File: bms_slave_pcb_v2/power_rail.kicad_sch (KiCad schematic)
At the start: 19 parts, among them Q13 2N7002, U5 LT3990HMSEI-5I-PBF

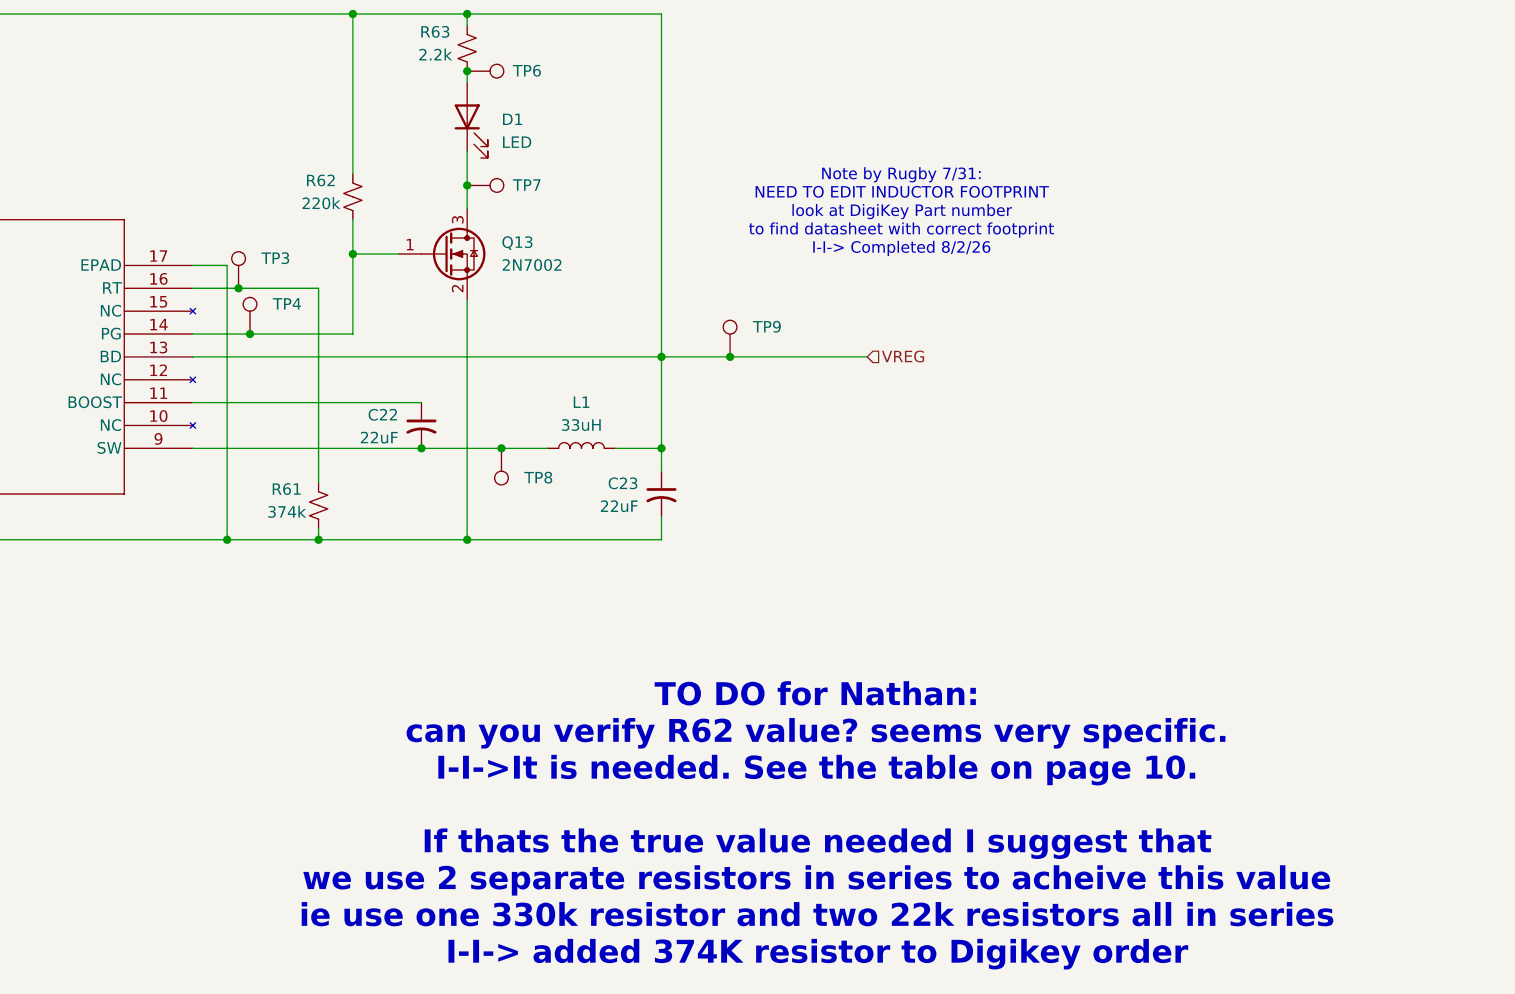
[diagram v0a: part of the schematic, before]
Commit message: Fixed filenames in BMS Slave PCB V2.01, added equipment wishlist
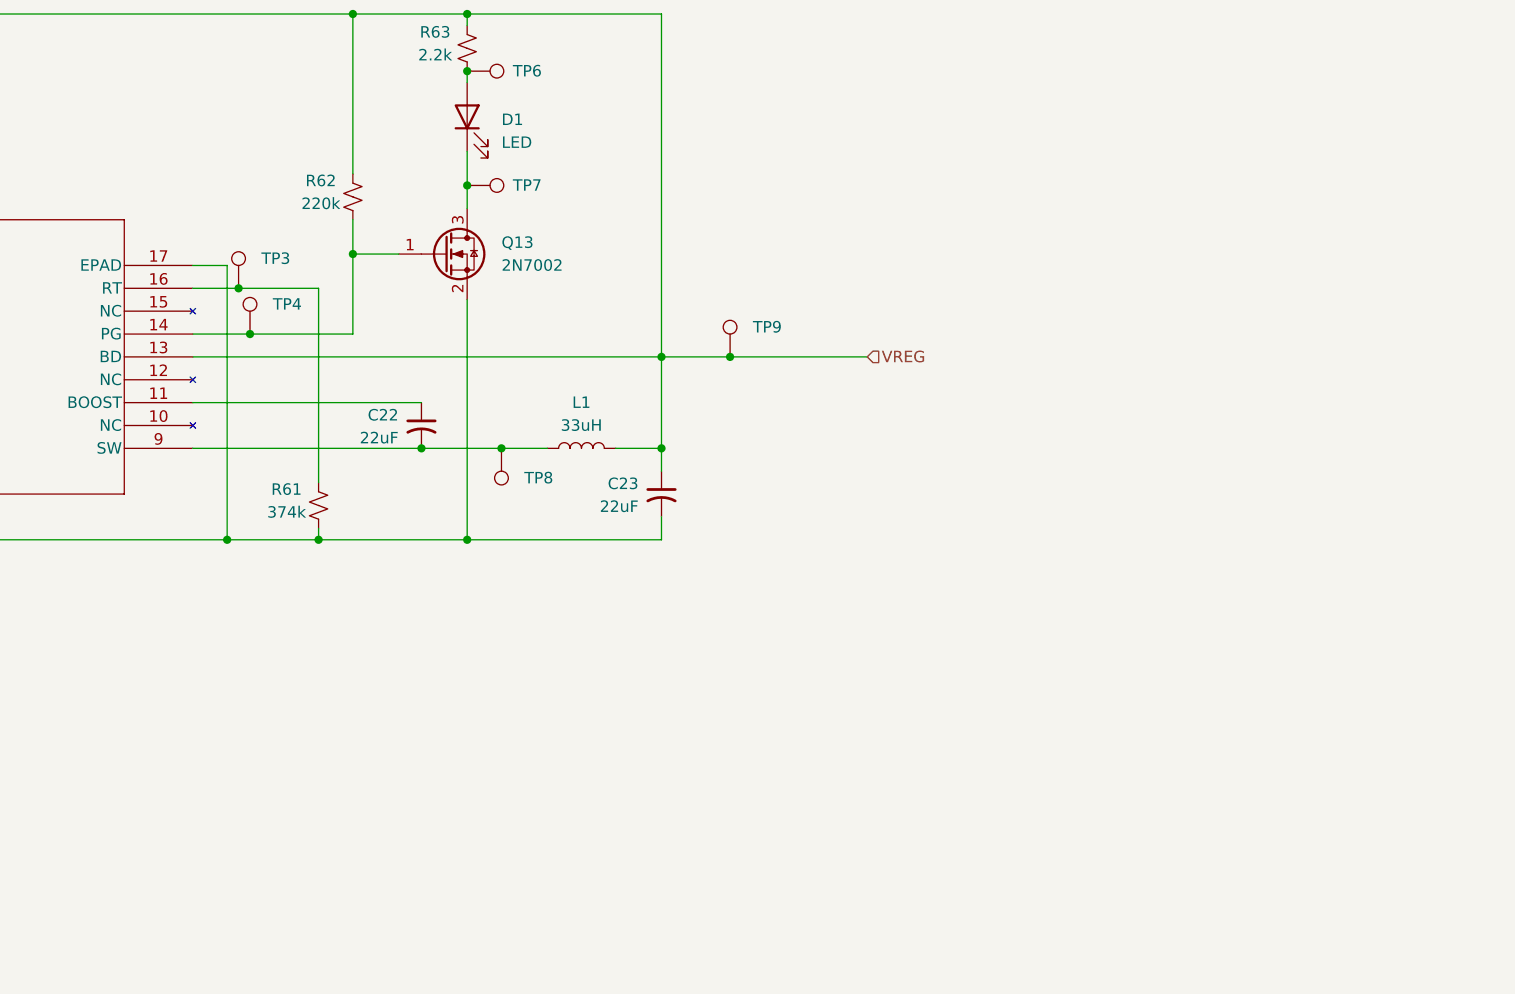
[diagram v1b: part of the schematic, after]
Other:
- note removed: "Note by Rugby 7/31: NEED TO EDIT INDUCTOR FOOTPRINT look at DigiKey Part number to find datasheet with correct footprint I-I-> Completed 8/2/26"
- note removed: "TO DO for Nathan: can you verify R62 value? seems very specific. I-I->It is needed. See the table on page 10. If thats the true value needed I suggest that we use 2 separate resistors in series to acheive this value ie use one 330k resistor and two 22k resistors all in series I-I-> added 374K resistor to Digikey order"
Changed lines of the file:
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@@
-		)
-	)
-	(text "Note by Rugby 7/31:\nNEED TO EDIT INDUCTOR FOOTPRINT\nlook at DigiKey Part number\nto find datasheet with correct footprint\nI-I-> Completed 8/2/26\n"
-		(exclude_from_sim no)
-		(at 220.98 77.978 0)
-		(effects
-			(font
-				(size 1.27 1.27)
-			)
-		)
-	)
-	(text "TO DO for Nathan:\ncan you verify R62 value? seems very specific.\nI-I->It is needed. See the table on page 10.\n\nIf thats the true value needed I suggest that\nwe use 2 separate resistors in series to acheive this value\nie use one 330k resistor and two 22k resistors all in series\nI-I-> added 374K resistor to Digikey order"
-		(exclude_from_sim no)
-		(at 211.582 146.05 0)
-		(effects
-			(font
-				(size 2.54 2.54)
-				(thickness 0.508)
-				(bold yes)
-			)
 		)
 	)
@@
 		)
 		(instances
-			(project "bms_slave_pcb"
+			(project "bms_slave_pcb_V2.01"
 				(path "/41ccf350-ee7b-4386-b0cf-c25b52556b27/21687209-543f-4328-b182-68e46d7f367b"
 					(reference "C21")
@@
 		)
 		(instances
-			(project "bms_slave_pcb"
+			(project "bms_slave_pcb_V2.01"
 				(path "/41ccf350-ee7b-4386-b0cf-c25b52556b27/21687209-543f-4328-b182-68e46d7f367b"
 					(reference "R63")
@@
 		)
 		(instances
-			(project "bms_slave_pcb"
+			(project "bms_slave_pcb_V2.01"
 				(path "/41ccf350-ee7b-4386-b0cf-c25b52556b27/21687209-543f-4328-b182-68e46d7f367b"
 					(reference "R61")
@@
 		)
 		(instances
-			(project "bms_slave_pcb"
+			(project "bms_slave_pcb_V2.01"
 				(path "/41ccf350-ee7b-4386-b0cf-c25b52556b27/21687209-543f-4328-b182-68e46d7f367b"
 					(reference "TP4")
@@
 		)
 		(instances
-			(project "bms_slave_pcb"
+			(project "bms_slave_pcb_V2.01"
 				(path "/41ccf350-ee7b-4386-b0cf-c25b52556b27/21687209-543f-4328-b182-68e46d7f367b"
 					(reference "TP3")
@@
 		)
 		(instances
-			(project "bms_slave_pcb"
+			(project "bms_slave_pcb_V2.01"
 				(path "/41ccf350-ee7b-4386-b0cf-c25b52556b27/21687209-543f-4328-b182-68e46d7f367b"
 					(reference "TP1")
@@
 		)
 		(instances
-			(project "bms_slave_pcb"
+			(project "bms_slave_pcb_V2.01"
 				(path "/41ccf350-ee7b-4386-b0cf-c25b52556b27/21687209-543f-4328-b182-68e46d7f367b"
 					(reference "U5")
@@
 		)
 		(instances
-			(project "bms_slave_pcb"
+			(project "bms_slave_pcb_V2.01"
 				(path "/41ccf350-ee7b-4386-b0cf-c25b52556b27/21687209-543f-4328-b182-68e46d7f367b"
 					(reference "R60")
@@
 		)
 		(instances
-			(project "bms_slave_pcb"
+			(project "bms_slave_pcb_V2.01"
 				(path "/41ccf350-ee7b-4386-b0cf-c25b52556b27/21687209-543f-4328-b182-68e46d7f367b"
 					(reference "TP2")
@@
 		)
 		(instances
-			(project "bms_slave_pcb"
+			(project "bms_slave_pcb_V2.01"
 				(path "/41ccf350-ee7b-4386-b0cf-c25b52556b27/21687209-543f-4328-b182-68e46d7f367b"
 					(reference "TP6")
@@
 		)
 		(instances
-			(project "bms_slave_pcb"
+			(project "bms_slave_pcb_V2.01"
 				(path "/41ccf350-ee7b-4386-b0cf-c25b52556b27/21687209-543f-4328-b182-68e46d7f367b"
 					(reference "C22")
@@
 		)
 		(instances
-			(project "bms_slave_pcb"
+			(project "bms_slave_pcb_V2.01"
 				(path "/41ccf350-ee7b-4386-b0cf-c25b52556b27/21687209-543f-4328-b182-68e46d7f367b"
 					(reference "R62")
@@
 		)
 		(instances
-			(project "bms_slave_pcb"
+			(project "bms_slave_pcb_V2.01"
 				(path "/41ccf350-ee7b-4386-b0cf-c25b52556b27/21687209-543f-4328-b182-68e46d7f367b"
 					(reference "TP7")
@@
 		)
 		(instances
-			(project "bms_slave_pcb"
+			(project "bms_slave_pcb_V2.01"
 				(path "/41ccf350-ee7b-4386-b0cf-c25b52556b27/21687209-543f-4328-b182-68e46d7f367b"
 					(reference "D1")
@@
 		)
 		(instances
-			(project "bms_slave_pcb"
+			(project "bms_slave_pcb_V2.01"
 				(path "/41ccf350-ee7b-4386-b0cf-c25b52556b27/21687209-543f-4328-b182-68e46d7f367b"
 					(reference "Q13")
@@
 		)
 		(instances
-			(project "bms_slave_pcb"
+			(project "bms_slave_pcb_V2.01"
 				(path "/41ccf350-ee7b-4386-b0cf-c25b52556b27/21687209-543f-4328-b182-68e46d7f367b"
 					(reference "L1")
@@
 		)
 		(instances
-			(project "bms_slave_pcb"
+			(project "bms_slave_pcb_V2.01"
 				(path "/41ccf350-ee7b-4386-b0cf-c25b52556b27/21687209-543f-4328-b182-68e46d7f367b"
 					(reference "C23")
@@
 		)
 		(instances
-			(project "bms_slave_pcb"
+			(project "bms_slave_pcb_V2.01"
 				(path "/41ccf350-ee7b-4386-b0cf-c25b52556b27/21687209-543f-4328-b182-68e46d7f367b"
 					(reference "TP8")
@@
 		)
 		(instances
-			(project "bms_slave_pcb"
+			(project "bms_slave_pcb_V2.01"
 				(path "/41ccf350-ee7b-4386-b0cf-c25b52556b27/21687209-543f-4328-b182-68e46d7f367b"
 					(reference "TP9")
@@
 		)
 		(instances
-			(project "bms_slave_pcb"
+			(project "bms_slave_pcb_V2.01"
 				(path "/41ccf350-ee7b-4386-b0cf-c25b52556b27/21687209-543f-4328-b182-68e46d7f367b"
 					(reference "#PWR041")
